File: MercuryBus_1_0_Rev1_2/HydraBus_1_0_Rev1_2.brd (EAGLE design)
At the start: 60 x 37 mm, 60 parts, among them IC1 STM32F405RGT, J1 CON_HEADER_2X06, J2 CON_HEADER_2X08, J3 CON_HEADER_2X08, J4 MICRO-SDCARD-CONNECTOR-330006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, J5 CON_HEADER_1X06-PTH, U1 IP4220CZ6, Y1_8MHZ 631-1100-ND, Y2_32.768KHZ 32.768KHz

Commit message: Fourth commit
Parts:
- added C17: 1uF, OPL:C0603
- added C18: 100nF, OPL:C0603
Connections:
- net +3V3: now also C17.2, C18.1
- net GND: now also C17.1, C18.2
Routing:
- net +3V3: track 229.8 -> 234.9 mm
- net VUSB: track 137.5 -> 138.2 mm
- net GND: track 43.2 -> 42.6 mm, vias 91 -> 97
- net PC10: vias 4 -> 2
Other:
- board text added: "(C) B.VERNOUX v1.0 Rev1_2+"
- board text removed: "(C) B.VERNOUX v1.0 Rev1_2"
- board text removed: "SPI2_MOSI"

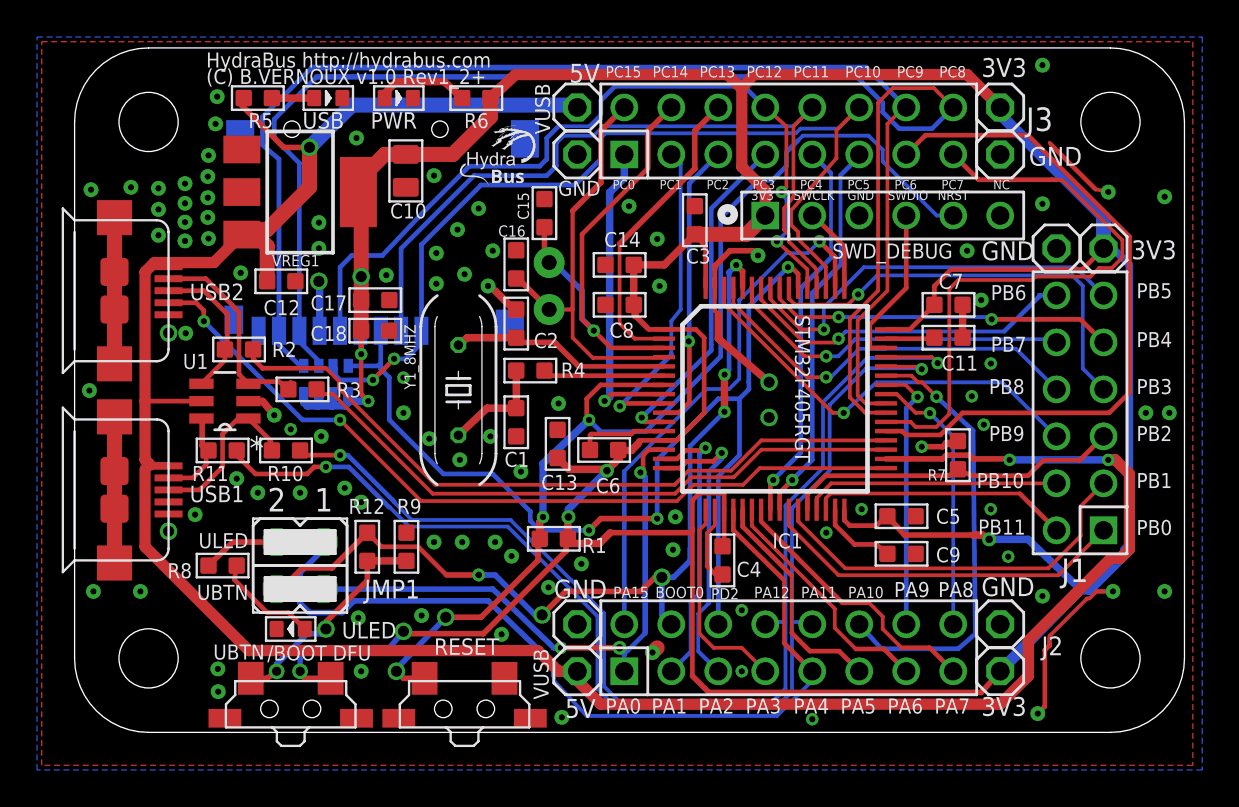
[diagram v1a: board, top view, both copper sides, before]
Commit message: Updated HydraBus_1_0_Rev1_2
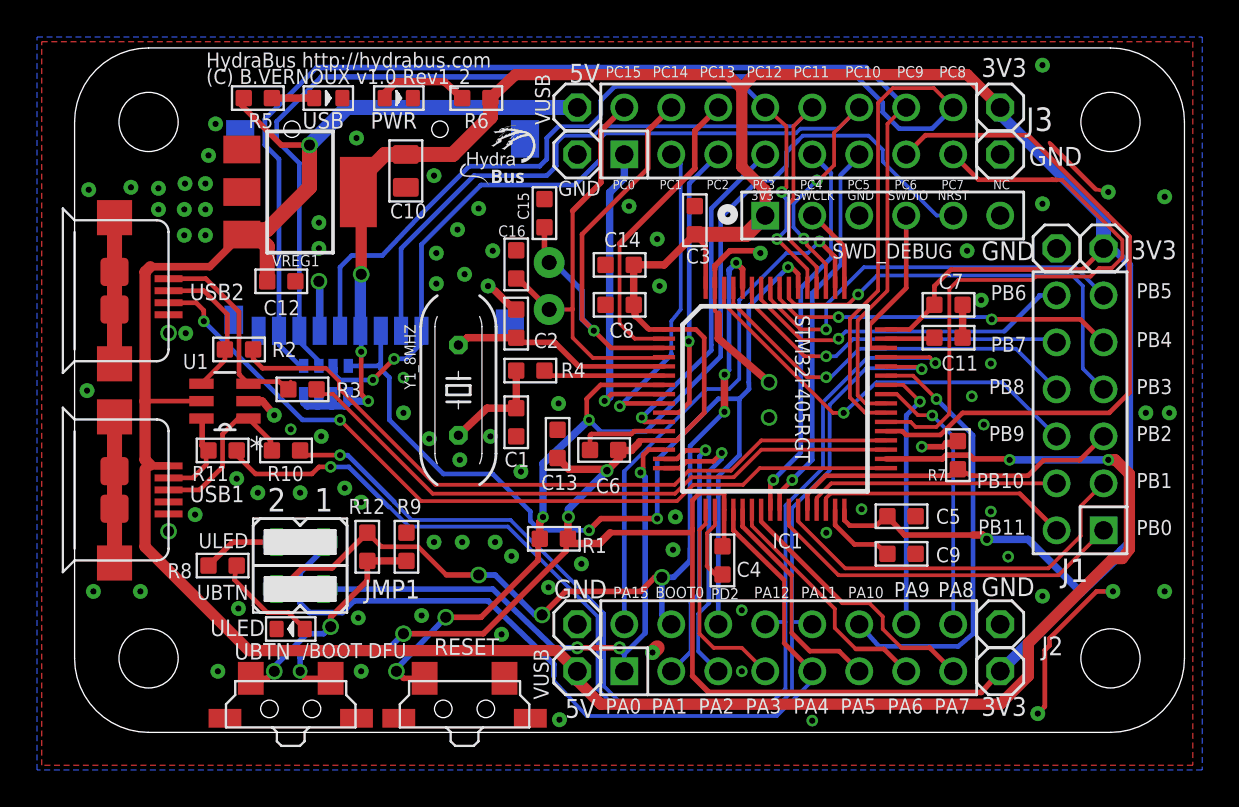
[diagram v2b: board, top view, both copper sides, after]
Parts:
- removed C17: 1uF, OPL:C0603
- removed C18: 100nF, OPL:C0603
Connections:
- net +3V3: no longer C17.2, C18.1
- net GND: no longer C17.1, C18.2
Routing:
- net +3V3: track 234.9 -> 229.8 mm
- net VUSB: track 138.2 -> 137.5 mm
- net GND: track 42.6 -> 43.2 mm, vias 97 -> 91
- net PC10: vias 2 -> 4
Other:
- board text added: "(C) B.VERNOUX v1.0 Rev1_2"
- board text added: "SPI2_MOSI"
- board text removed: "(C) B.VERNOUX v1.0 Rev1_2+"
